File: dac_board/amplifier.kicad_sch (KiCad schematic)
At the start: 29 parts

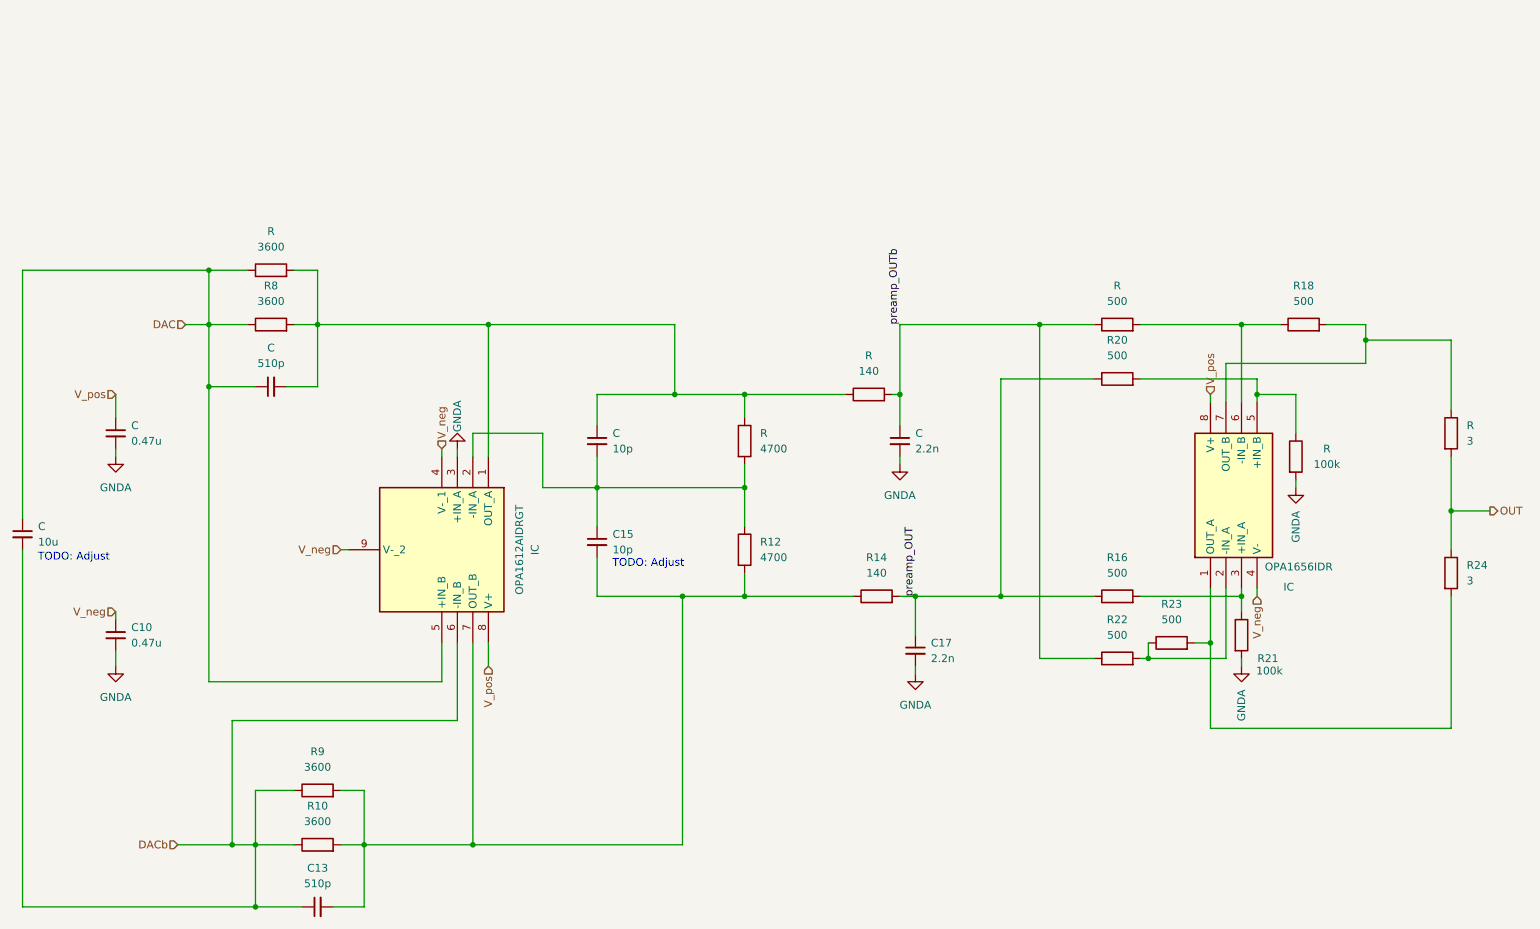
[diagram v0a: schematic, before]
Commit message: Additional work on DAC
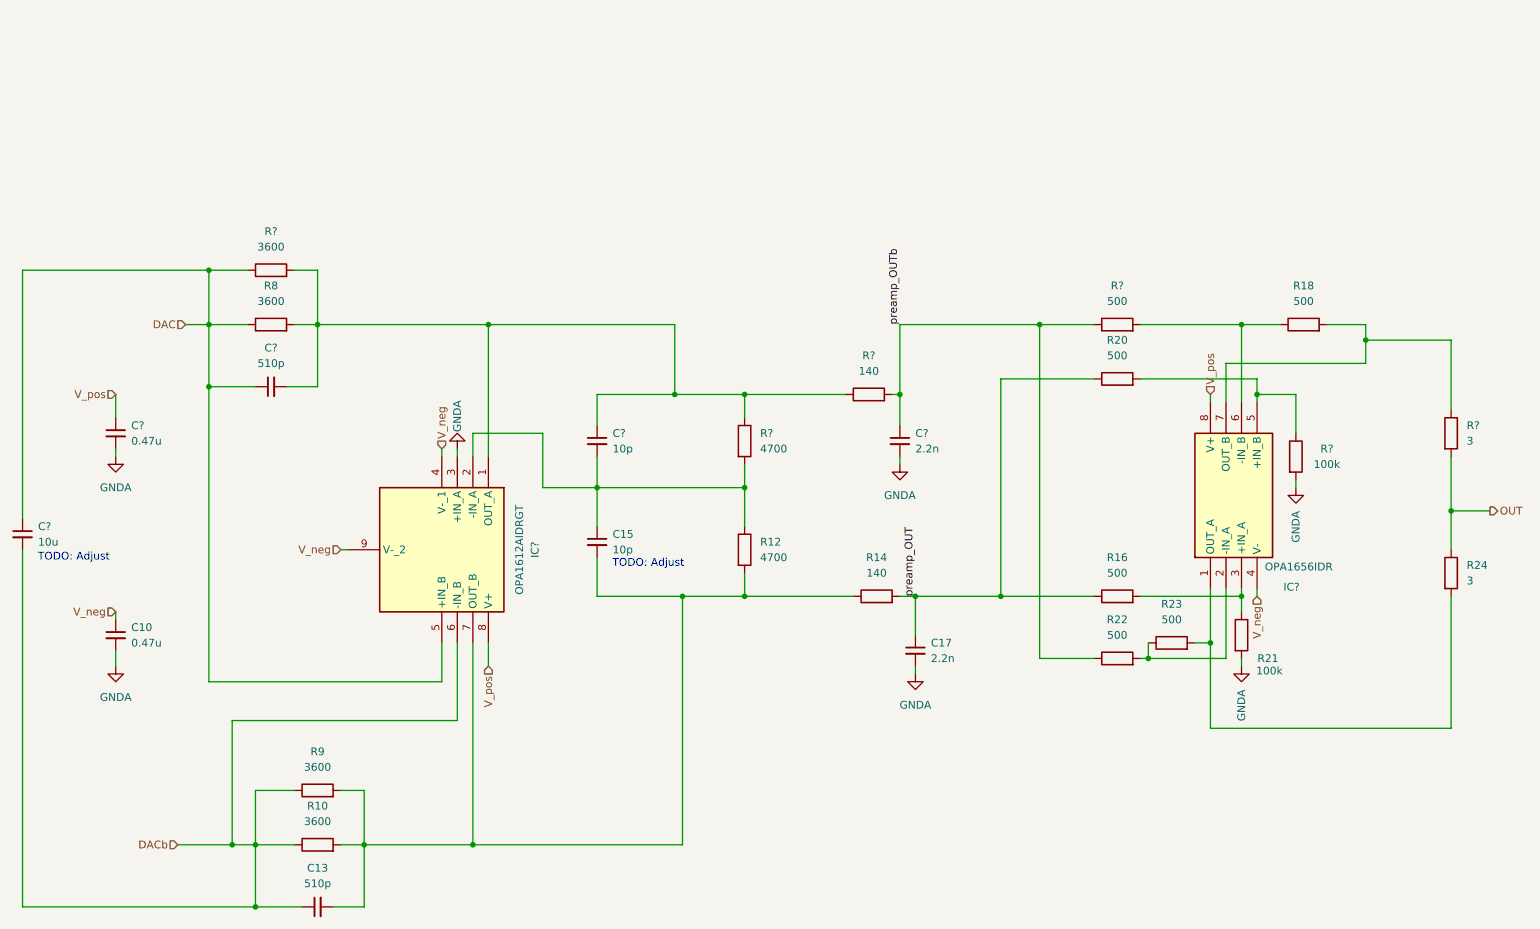
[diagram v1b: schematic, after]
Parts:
- renumbered C to C?, IC to IC?, R to R?
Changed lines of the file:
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@@
 		(dnp no)
 		(fields_autoplaced yes)
-		(property "Reference" "#PWR"
+		(property "Reference" "#PWR?"
 			(at 33.02 96.52 0)
 			(effects
@@
 		(instances
 			(project "dac_board"
+				(path "/387b6079-e547-4b62-84b5-51a54c04db0a/6d234bbe-76d5-4bb0-ba16-fed298a9d9f4"
+					(reference "#PWR?")
+					(unit 1)
+				)
 				(path "/387b6079-e547-4b62-84b5-51a54c04db0a/a874625f-e1b7-4234-b951-45cc10abb286"
 					(reference "#PWR025")
@@
 		(dnp no)
 		(fields_autoplaced yes)
-		(property "Reference" "C"
+		(property "Reference" "C?"
 			(at 58.4263 72.39 90)
 			(effects
@@
 		(instances
 			(project "dac_board"
+				(path "/387b6079-e547-4b62-84b5-51a54c04db0a/6d234bbe-76d5-4bb0-ba16-fed298a9d9f4"
+					(reference "C?")
+					(unit 1)
+				)
 				(path "/387b6079-e547-4b62-84b5-51a54c04db0a/a874625f-e1b7-4234-b951-45cc10abb286"
 					(reference "C21")
@@
 		(dnp no)
 		(fields_autoplaced yes)
-		(property "Reference" "C"
+		(property "Reference" "C?"
 			(at 35.56 85.0962 0)
 			(effects
@@
 		(instances
 			(project "dac_board"
+				(path "/387b6079-e547-4b62-84b5-51a54c04db0a/6d234bbe-76d5-4bb0-ba16-fed298a9d9f4"
+					(reference "C?")
+					(unit 1)
+				)
 				(path "/387b6079-e547-4b62-84b5-51a54c04db0a/a874625f-e1b7-4234-b951-45cc10abb286"
 					(reference "C19")
@@
 		(dnp no)
 		(fields_autoplaced yes)
-		(property "Reference" "R"
+		(property "Reference" "R?"
 			(at 156.21 73.66 90)
 			(effects
@@
 		(instances
 			(project "dac_board"
+				(path "/387b6079-e547-4b62-84b5-51a54c04db0a/6d234bbe-76d5-4bb0-ba16-fed298a9d9f4"
+					(reference "R?")
+					(unit 1)
+				)
 				(path "/387b6079-e547-4b62-84b5-51a54c04db0a/a874625f-e1b7-4234-b951-45cc10abb286"
 					(reference "R31")
@@
 		(dnp no)
 		(fields_autoplaced yes)
-		(property "Reference" "R"
+		(property "Reference" "R?"
 			(at 196.85 62.23 90)
 			(effects
@@
 		(instances
 			(project "dac_board"
+				(path "/387b6079-e547-4b62-84b5-51a54c04db0a/6d234bbe-76d5-4bb0-ba16-fed298a9d9f4"
+					(reference "R?")
+					(unit 1)
+				)
 				(path "/387b6079-e547-4b62-84b5-51a54c04db0a/a874625f-e1b7-4234-b951-45cc10abb286"
 					(reference "R33")
@@
 		(dnp no)
 		(fields_autoplaced yes)
-		(property "Reference" "C"
+		(property "Reference" "C?"
 			(at 163.83 86.3662 0)
 			(effects
@@
 		(instances
 			(project "dac_board"
+				(path "/387b6079-e547-4b62-84b5-51a54c04db0a/6d234bbe-76d5-4bb0-ba16-fed298a9d9f4"
+					(reference "C?")
+					(unit 1)
+				)
 				(path "/387b6079-e547-4b62-84b5-51a54c04db0a/a874625f-e1b7-4234-b951-45cc10abb286"
 					(reference "C25")
@@
 		(dnp no)
 		(fields_autoplaced yes)
-		(property "Reference" "C"
+		(property "Reference" "C?"
 			(at 20.32 101.6062 0)
 			(effects
@@
 		(instances
 			(project "dac_board"
+				(path "/387b6079-e547-4b62-84b5-51a54c04db0a/6d234bbe-76d5-4bb0-ba16-fed298a9d9f4"
+					(reference "C?")
+					(unit 1)
+				)
 				(path "/387b6079-e547-4b62-84b5-51a54c04db0a/a874625f-e1b7-4234-b951-45cc10abb286"
 					(reference "C18")
@@
 		(dnp no)
 		(fields_autoplaced yes)
-		(property "Reference" "R"
+		(property "Reference" "R?"
 			(at 58.42 53.34 90)
 			(effects
@@
 		(instances
 			(project "dac_board"
+				(path "/387b6079-e547-4b62-84b5-51a54c04db0a/6d234bbe-76d5-4bb0-ba16-fed298a9d9f4"
+					(reference "R?")
+					(unit 1)
+				)
 				(path "/387b6079-e547-4b62-84b5-51a54c04db0a/a874625f-e1b7-4234-b951-45cc10abb286"
 					(reference "R25")
@@
 		(dnp no)
 		(fields_autoplaced yes)
-		(property "Reference" "IC"
+		(property "Reference" "IC?"
 			(at 101.6 105.41 0)
 			(effects
@@
 		(instances
 			(project "dac_board"
+				(path "/387b6079-e547-4b62-84b5-51a54c04db0a/6d234bbe-76d5-4bb0-ba16-fed298a9d9f4"
+					(reference "IC?")
+					(unit 1)
+				)
 				(path "/387b6079-e547-4b62-84b5-51a54c04db0a/a874625f-e1b7-4234-b951-45cc10abb286"
 					(reference "IC3")
@@
 		(on_board yes)
 		(dnp no)
-		(property "Reference" "#PWR"
+		(property "Reference" "#PWR?"
 			(at 88.9 82.55 0)
 			(effects
@@
 		(instances
 			(project "dac_board"
+				(path "/387b6079-e547-4b62-84b5-51a54c04db0a/6d234bbe-76d5-4bb0-ba16-fed298a9d9f4"
+					(reference "#PWR?")
+					(unit 1)
+				)
 				(path "/387b6079-e547-4b62-84b5-51a54c04db0a/a874625f-e1b7-4234-b951-45cc10abb286"
 					(reference "#PWR027")
@@
 		(dnp no)
 		(fields_autoplaced yes)
-		(property "Reference" "#PWR"
+		(property "Reference" "#PWR?"
 			(at 226.06 101.6 0)
 			(effects
@@
 		(instances
 			(project "dac_board"
+				(path "/387b6079-e547-4b62-84b5-51a54c04db0a/6d234bbe-76d5-4bb0-ba16-fed298a9d9f4"
+					(reference "#PWR?")
+					(unit 1)
+				)
 				(path "/387b6079-e547-4b62-84b5-51a54c04db0a/a874625f-e1b7-4234-b951-45cc10abb286"
 					(reference "#PWR031")
@@
 		(dnp no)
 		(fields_autoplaced yes)
-		(property "Reference" "#PWR"
+		(property "Reference" "#PWR?"
 			(at 163.83 132.08 0)
 			(effects
@@
 		(instances
 			(project "dac_board"
+				(path "/387b6079-e547-4b62-84b5-51a54c04db0a/6d234bbe-76d5-4bb0-ba16-fed298a9d9f4"
+					(reference "#PWR?")
+					(unit 1)
+				)
 				(path "/387b6079-e547-4b62-84b5-51a54c04db0a/a874625f-e1b7-4234-b951-45cc10abb286"
 					(reference "#PWR029")
@@
 		(on_board yes)
 		(dnp no)
-		(property "Reference" "IC"
+		(property "Reference" "IC?"
 			(at 224.028 111.506 90)
 			(effects
@@
 		(instances
 			(project "dac_board"
+				(path "/387b6079-e547-4b62-84b5-51a54c04db0a/6d234bbe-76d5-4bb0-ba16-fed298a9d9f4"
+					(reference "IC?")
+					(unit 1)
+				)
 				(path "/387b6079-e547-4b62-84b5-51a54c04db0a/a874625f-e1b7-4234-b951-45cc10abb286"
 					(reference "IC4")
@@
 		(dnp no)
 		(fields_autoplaced yes)
-		(property "Reference" "R"
+		(property "Reference" "R?"
 			(at 138.43 86.3599 0)
 			(effects
@@
 		(instances
 			(project "dac_board"
+				(path "/387b6079-e547-4b62-84b5-51a54c04db0a/6d234bbe-76d5-4bb0-ba16-fed298a9d9f4"
+					(reference "R?")
+					(unit 1)
+				)
 				(path "/387b6079-e547-4b62-84b5-51a54c04db0a/a874625f-e1b7-4234-b951-45cc10abb286"
 					(reference "R29")
@@
 		(dnp no)
 		(fields_autoplaced yes)
-		(property "Reference" "#PWR"
+		(property "Reference" "#PWR?"
 			(at 161.29 97.79 0)
 			(effects
@@
 		(instances
 			(project "dac_board"
+				(path "/387b6079-e547-4b62-84b5-51a54c04db0a/6d234bbe-76d5-4bb0-ba16-fed298a9d9f4"
+					(reference "#PWR?")
+					(unit 1)
+				)
 				(path "/387b6079-e547-4b62-84b5-51a54c04db0a/a874625f-e1b7-4234-b951-45cc10abb286"
 					(reference "#PWR028")
@@
 		(on_board yes)
 		(dnp no)
-		(property "Reference" "R"
+		(property "Reference" "R?"
 			(at 231.14 88.9 0)
 			(effects
@@
 		(instances
 			(project "dac_board"
+				(path "/387b6079-e547-4b62-84b5-51a54c04db0a/6d234bbe-76d5-4bb0-ba16-fed298a9d9f4"
+					(reference "R?")
+					(unit 1)
+				)
 				(path "/387b6079-e547-4b62-84b5-51a54c04db0a/a874625f-e1b7-4234-b951-45cc10abb286"
 					(reference "R39")
@@
 		(dnp no)
 		(fields_autoplaced yes)
-		(property "Reference" "C"
+		(property "Reference" "C?"
 			(at 114.3 86.3662 0)
 			(effects
@@
 		(instances
 			(project "dac_board"
+				(path "/387b6079-e547-4b62-84b5-51a54c04db0a/6d234bbe-76d5-4bb0-ba16-fed298a9d9f4"
+					(reference "C?")
+					(unit 1)
+				)
 				(path "/387b6079-e547-4b62-84b5-51a54c04db0a/a874625f-e1b7-4234-b951-45cc10abb286"
 					(reference "C23")
@@
 		(dnp no)
 		(fields_autoplaced yes)
-		(property "Reference" "R"
+		(property "Reference" "R?"
 			(at 254 85.0899 0)
 			(effects
@@
 		(instances
 			(project "dac_board"
+				(path "/387b6079-e547-4b62-84b5-51a54c04db0a/6d234bbe-76d5-4bb0-ba16-fed298a9d9f4"
+					(reference "R?")
+					(unit 1)
+				)
 				(path "/387b6079-e547-4b62-84b5-51a54c04db0a/a874625f-e1b7-4234-b951-45cc10abb286"
 					(reference "R41")

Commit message: More updates, finished DAC block
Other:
- title: (none) -> Amplifier
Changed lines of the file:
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@@
 	(generator_version "9.0")
 	(paper "A4")
+	(title_block
+		(title "Amplifier")
+	)
 	(text "TODO: Adjust"
 		(exclude_from_sim no)

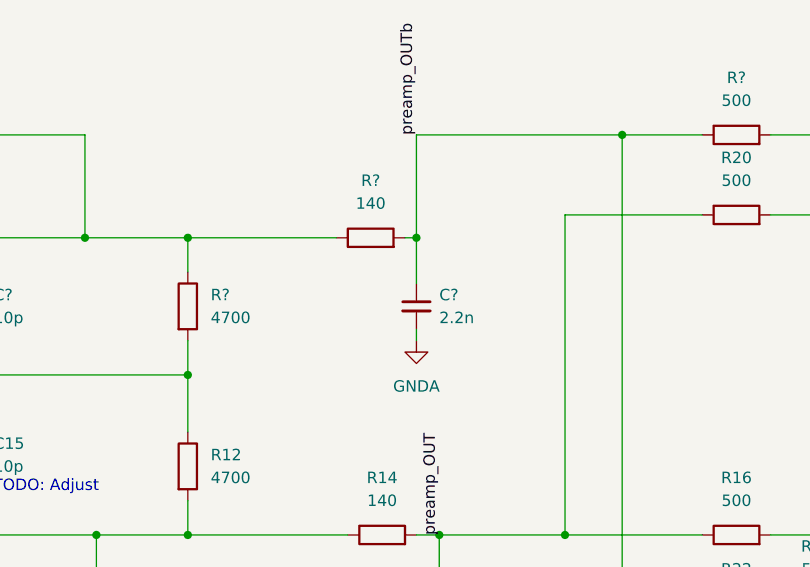
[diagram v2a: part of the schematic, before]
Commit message: Updated schematic with detailed info from SPICE simulations
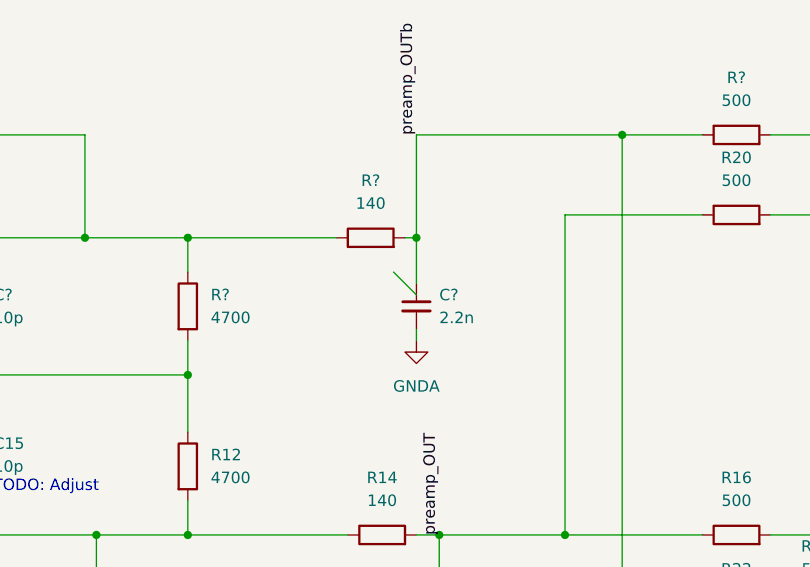
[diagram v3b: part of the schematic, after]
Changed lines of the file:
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@@
 		(color 0 0 0 0)
+	)
+	(bus_entry
+		(at 158.75 83.82)
+		(size 2.54 2.54)
+		(stroke
+			(width 0)
+			(type default)
+		)
 	)
 	(wire

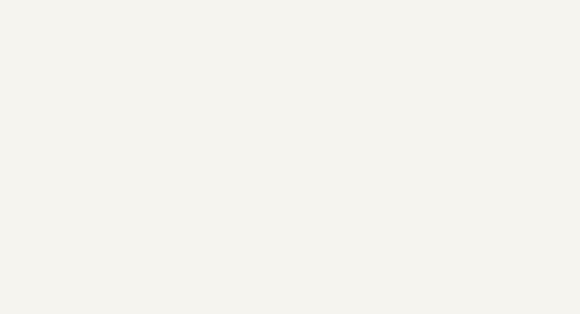
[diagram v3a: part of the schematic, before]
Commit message: Finished schematic design for MCU + DAC
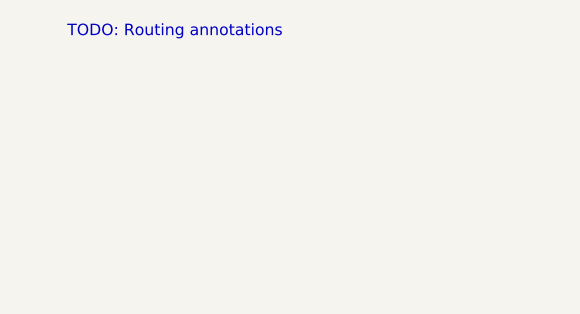
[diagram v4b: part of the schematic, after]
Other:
- note added: "TODO: Routing annotations"
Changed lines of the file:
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@@
+		)
+	)
+	(text "TODO: Routing annotations"
+		(exclude_from_sim no)
+		(at 33.528 19.05 0)
+		(effects
+			(font
+				(size 1.27 1.27)
+			)
 		)
 	)
